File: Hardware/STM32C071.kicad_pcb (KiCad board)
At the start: 2 copper layers, 50 x 25 mm, 16 parts, among them J1 USB_C_Receptacle_USB2.0_16P, J2 Conn_01x04_Pin, U1 STM32C071K8Tx, U2 USBLC6-2P6, U4 XL1509-ADJE1

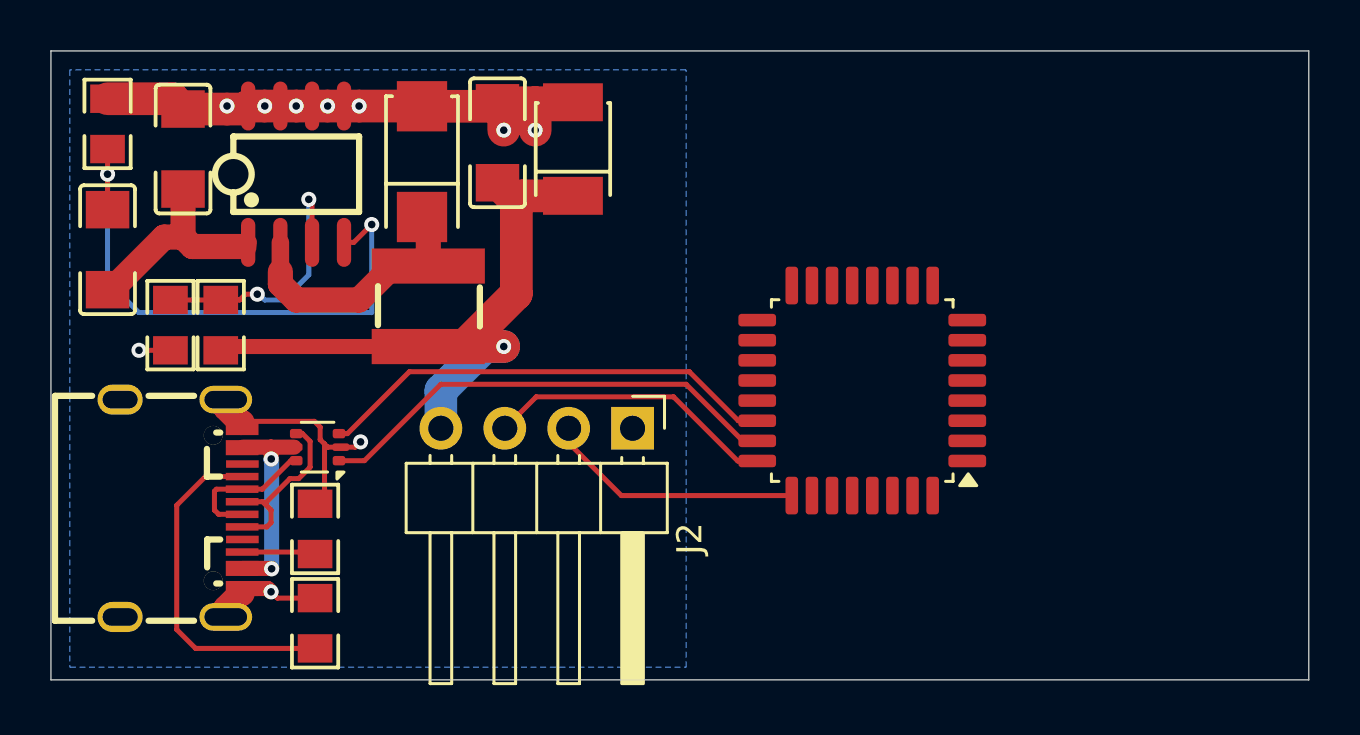
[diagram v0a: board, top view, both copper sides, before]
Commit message: Added Reset and power connections, 45 rotation
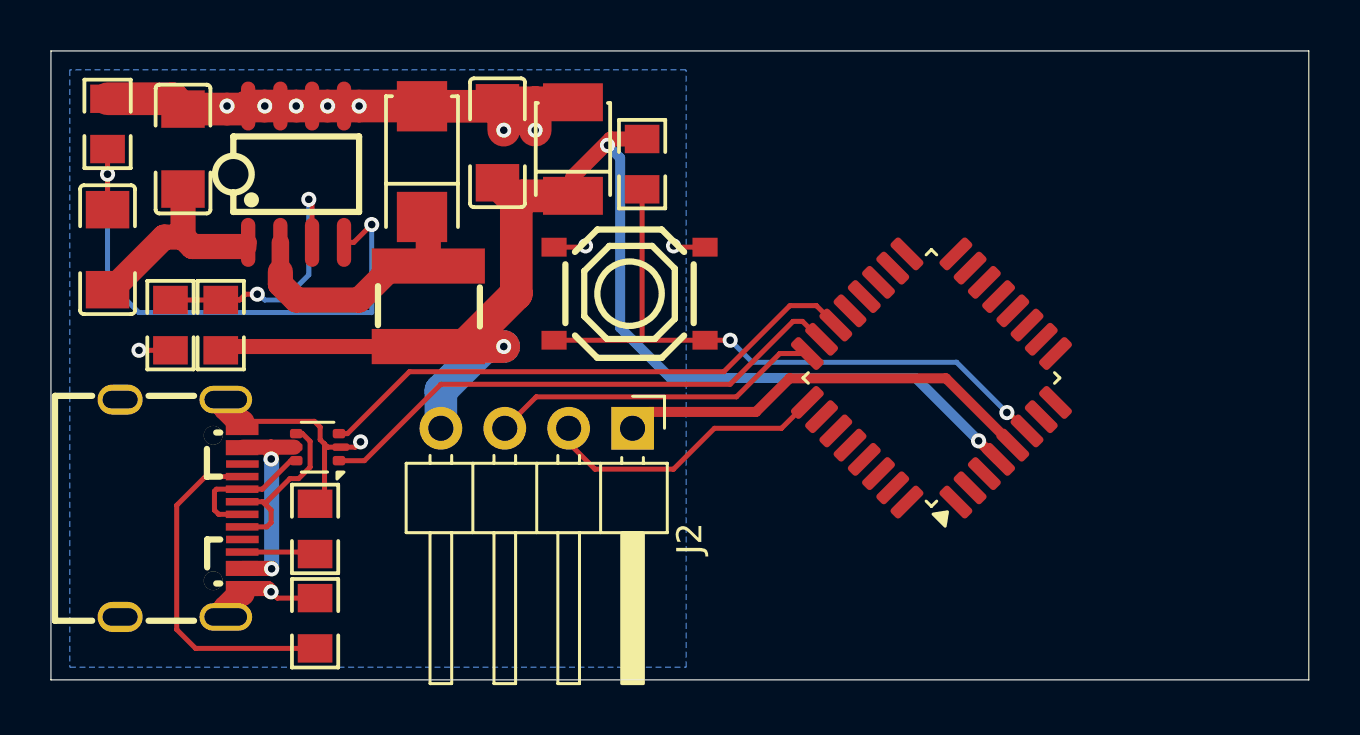
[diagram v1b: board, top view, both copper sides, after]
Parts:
- added R6: 22kΩ, jlcbasic:R0805, F.Cu at (123.5, 79.5)
- added SW1: TS-1187A-B-A-B, jlcbasic:SW-SMD_4P-L5.1-W5.1-P3.70-LS6.5-TL_H1.5, F.Cu at (123.0, 84.7)
- moved U1 2.80 mm to (135.0, 88.0), turned to 135 degrees
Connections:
- U1 pad 6: unconnected-(U1-PF2-Pad6) -> NRST
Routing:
- net +3.3V: track 27.5 -> 56.3 mm, vias 1 -> 3
- net NRST: track 0.00 -> 26.3 mm, vias 0 -> 2
- net GND: track 36.0 -> 55.6 mm, vias 10 -> 12
- net Net-(U1-PA11): track 18.5 -> 22.2 mm
- net Net-(U1-PA12): track 18.8 -> 21.8 mm
- net Net-(J2-Pin_3): track 11.6 -> 13.3 mm
- net Net-(J2-Pin_2): track 10.3 -> 11.6 mm
